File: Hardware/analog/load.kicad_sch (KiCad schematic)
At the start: 41 parts

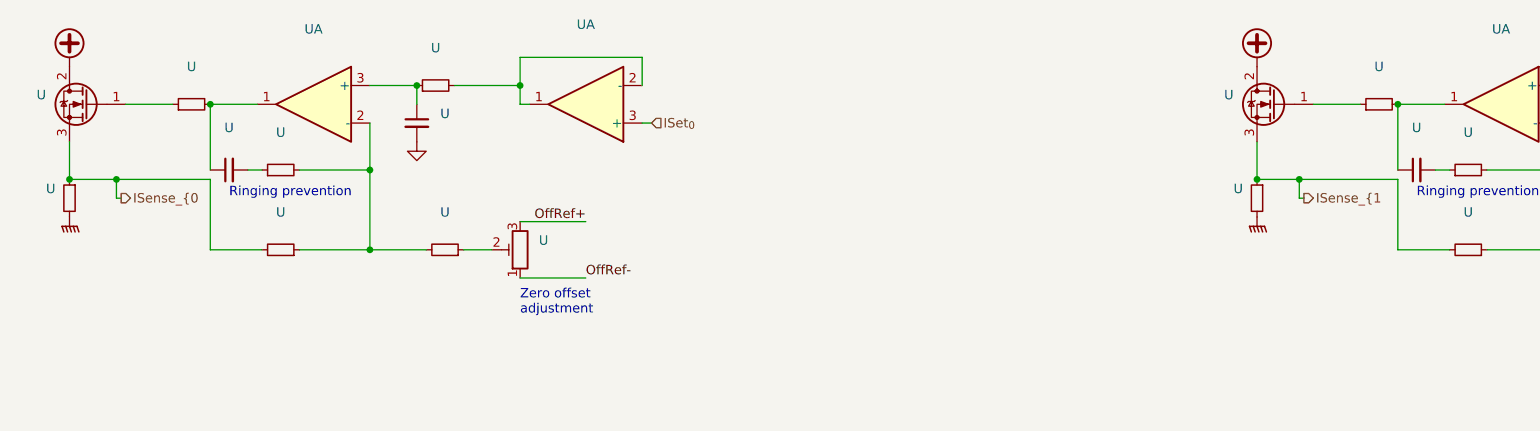
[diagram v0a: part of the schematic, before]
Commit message: Analog board tweaks
- Moved a few traces and components around to accomodate other changes
  in the controller stuff, preparation for some sort of cleanup

- Aesthetic moves of labels on controller board
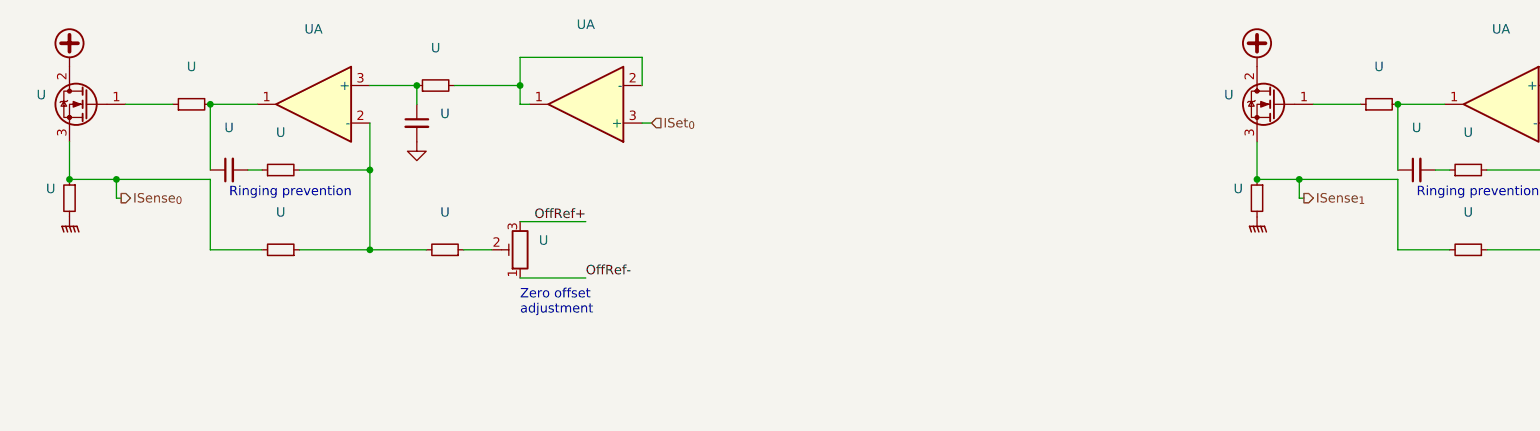
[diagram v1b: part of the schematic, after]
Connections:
- net ISense_{0 renamed ISense_{0}
- net ISense_{1 renamed ISense_{1}
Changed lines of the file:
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@@
     (effects (font (size 1.27 1.27)) (justify left))
   )
-  (hierarchical_label "ISense_{0" (shape output) (at 39.37 43.18 0) (fields_autoplaced)
+  (hierarchical_label "ISense_{0}" (shape output) (at 39.37 43.18 0) (fields_autoplaced)
     (effects (font (size 1.27 1.27)) (justify left))
   )
-  (hierarchical_label "ISense_{1" (shape output) (at 199.39 43.18 0) (fields_autoplaced)
+  (hierarchical_label "ISense_{1}" (shape output) (at 199.39 43.18 0) (fields_autoplaced)
     (effects (font (size 1.27 1.27)) (justify left))
   )

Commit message: Mostly finished up analog load board
- Finished routing most signals

- Connected relay drive to bonus I2C GPIO controller, and routed the
  rest of the voltage sense stuff

- Routed the reset signal to the DAC, so that when the board is reset,
  the current output will be reset to zero as well without processor
  intervention

- Replaced most passives with 0603/1608 size
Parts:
- U: MPN CR0805-JW-102ELF -> (none)
- U: MPN WR08X101-JTL -> (none)
- U: MPN 260-4.7M-RC -> (none)
- U: MPN CL21B223KBANNNC -> (none)
- U: MPN CR0805-FX-4991ELF -> (none)
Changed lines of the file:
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@@
       (effects (font (size 1.27 1.27)) hide)
     )
-    (property "MPN" "CR0805-JW-102ELF" (id 4) (at 60.96 39.37 90)
+    (property "MPN" "" (id 4) (at 60.96 39.37 90)
       (effects (font (size 1.27 1.27)) hide)
     )
@@
       (effects (font (size 1.27 1.27)) hide)
     )
-    (property "MPN" "CR0805-JW-102ELF" (id 4) (at 221.615 50.165 90)
+    (property "MPN" "" (id 4) (at 221.615 50.165 90)
       (effects (font (size 1.27 1.27)) hide)
     )
@@
       (effects (font (size 1.27 1.27)) hide)
     )
-    (property "MPN" "WR08X101-JTL" (id 4) (at 209.55 30.48 90)
+    (property "MPN" "" (id 4) (at 209.55 30.48 90)
       (effects (font (size 1.27 1.27)) hide)
     )
@@
       (effects (font (size 1.27 1.27)) hide)
     )
-    (property "MPN" "CR0805-JW-102ELF" (id 4) (at 221.615 39.37 90)
+    (property "MPN" "" (id 4) (at 221.615 39.37 90)
       (effects (font (size 1.27 1.27)) hide)
     )
@@
       (effects (font (size 1.27 1.27)) hide)
     )
-    (property "MPN" "260-4.7M-RC" (id 4) (at 243.84 50.165 90)
+    (property "MPN" "" (id 4) (at 243.84 50.165 90)
       (effects (font (size 1.27 1.27)) hide)
     )
@@
       (effects (font (size 1.27 1.27)) hide)
     )
-    (property "MPN" "CL21B223KBANNNC" (id 4) (at 79.375 33.02 0)
+    (property "MPN" "" (id 4) (at 79.375 33.02 0)
       (effects (font (size 1.27 1.27)) hide)
     )
@@
       (effects (font (size 1.27 1.27)) hide)
     )
-    (property "MPN" "CR0805-FX-4991ELF" (id 4) (at 81.915 27.94 90)
+    (property "MPN" "" (id 4) (at 81.915 27.94 90)
       (effects (font (size 1.27 1.27)) hide)
     )
@@
       (effects (font (size 1.27 1.27)) hide)
     )
-    (property "MPN" "CR0805-JW-102ELF" (id 4) (at 60.96 50.165 90)
+    (property "MPN" "" (id 4) (at 60.96 50.165 90)
       (effects (font (size 1.27 1.27)) hide)
     )
@@
       (effects (font (size 1.27 1.27)) hide)
     )
-    (property "MPN" "CR0805-FX-4991ELF" (id 4) (at 242.57 27.94 90)
+    (property "MPN" "" (id 4) (at 242.57 27.94 90)
       (effects (font (size 1.27 1.27)) hide)
     )
@@
       (effects (font (size 1.27 1.27)) hide)
     )
-    (property "MPN" "WR08X101-JTL" (id 4) (at 48.895 30.48 90)
+    (property "MPN" "" (id 4) (at 48.895 30.48 90)
       (effects (font (size 1.27 1.27)) hide)
     )
@@
       (effects (font (size 1.27 1.27)) hide)
     )
-    (property "MPN" "CL21B223KBANNNC" (id 4) (at 240.03 33.02 0)
+    (property "MPN" "" (id 4) (at 240.03 33.02 0)
       (effects (font (size 1.27 1.27)) hide)
     )
@@
       (effects (font (size 1.27 1.27)) hide)
     )
-    (property "MPN" "CR0805-JW-102ELF" (id 4) (at 123.825 139.065 0)
+    (property "MPN" "" (id 4) (at 123.825 139.065 0)
       (effects (font (size 1.27 1.27)) hide)
     )
@@
       (effects (font (size 1.27 1.27)) hide)
     )
-    (property "MPN" "CR0805-JW-102ELF" (id 4) (at 101.6 139.065 0)
+    (property "MPN" "" (id 4) (at 101.6 139.065 0)
       (effects (font (size 1.27 1.27)) hide)
     )
@@
       (effects (font (size 1.27 1.27)) hide)
     )
-    (property "MPN" "260-4.7M-RC" (id 4) (at 83.185 50.165 90)
-      (effects (font (size 1.27 1.27)) hide)
-    )
+    (property "MPN" "" (id 4) (at 83.185 50.165 90)
+      (effects (font (size 1.27 1.27)) hide)
+    )

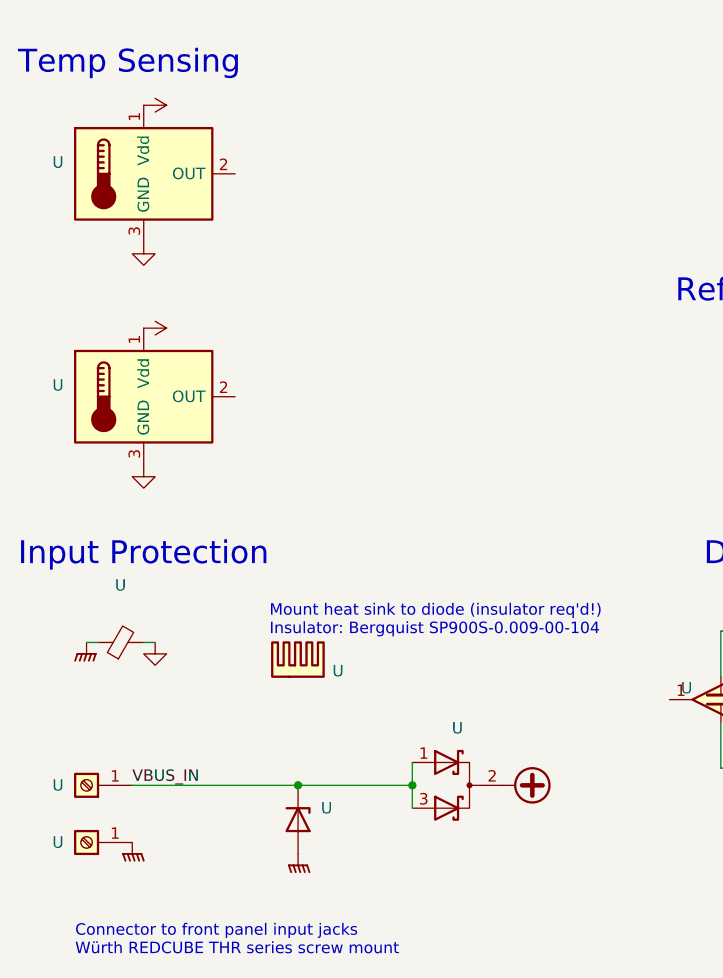
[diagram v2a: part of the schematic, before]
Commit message: Temperature sensing & cleanup for analog board
- Added the auxiliary temperature sensing ADC, and routed it to the
  analog temperature sensors on the front and rear of the MOSFET
  heatsink

- Added an LM75 sensor to measure the analog board ambient temperature
  (for better temperature control/fan control)

  This may end up being a DNP item if it's not really useful or
  otherwise necessary.

- Fixes to a few symbols (namely pin directions) to pass ERC
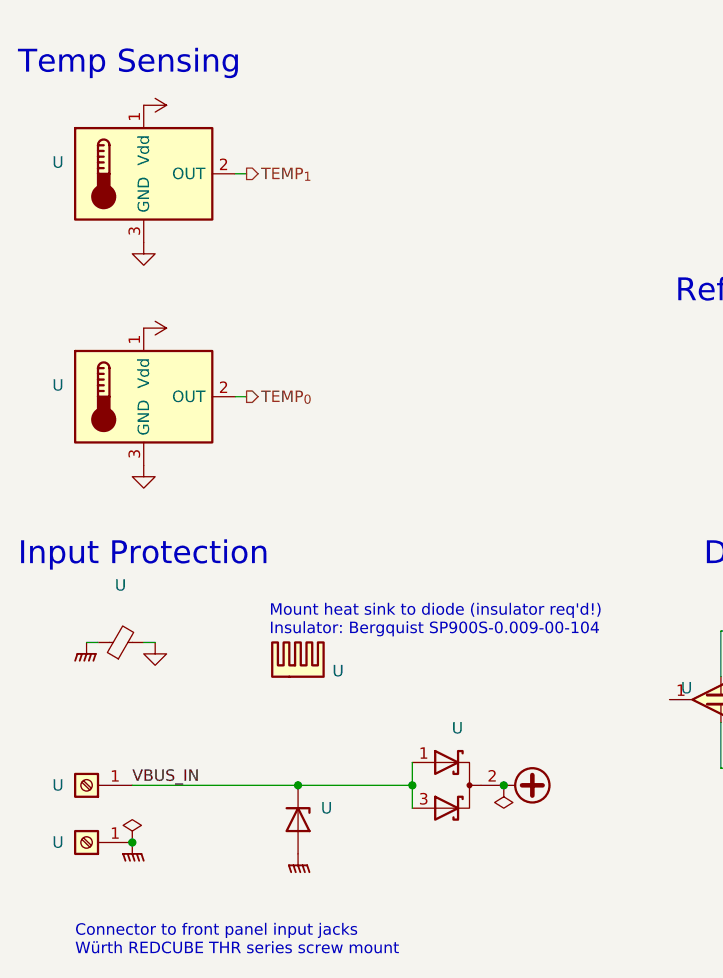
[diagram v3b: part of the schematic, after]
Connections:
- net TEMP_{1}: now reaches U.2 (OUT)
- net TEMP_{0}: now reaches U.2 (OUT)
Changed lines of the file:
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@@
   (junction (at 123.825 136.525) (diameter 0) (color 0 0 0 0)
   )
+  (junction (at 73.025 176.53) (diameter 0) (color 0 0 0 0)
+  )
   (junction (at 240.03 27.94) (diameter 0) (color 0 0 0 0)
   )
   (junction (at 51.435 30.48) (diameter 0) (color 0 0 0 0)
   )
+  (junction (at 31.75 182.88) (diameter 0) (color 0 0 0 0)
+  )
   (junction (at 93.345 27.94) (diameter 0) (color 0 0 0 0)
   )
@@
     (stroke (width 0) (type default))
   )
+  (wire (pts (xy 43.18 133.35) (xy 44.45 133.35))
+    (stroke (width 0) (type default))
+  )
   (wire (pts (xy 79.375 27.94) (xy 79.375 30.48))
     (stroke (width 0) (type default))
@@
   )
   (wire (pts (xy 73.025 39.37) (xy 73.025 50.165))
+    (stroke (width 0) (type default))
+  )
+  (wire (pts (xy 43.18 108.585) (xy 44.45 108.585))
     (stroke (width 0) (type default))
   )
@@
     (effects (font (size 1.27 1.27)) (justify left))
   )
+  (hierarchical_label "TEMP_{1}" (shape output) (at 44.45 108.585 0) (fields_autoplaced)
+    (effects (font (size 1.27 1.27)) (justify left))
+  )
   (hierarchical_label "ISense_{0}" (shape output) (at 39.37 43.18 0) (fields_autoplaced)
+    (effects (font (size 1.27 1.27)) (justify left))
+  )
+  (hierarchical_label "TEMP_{0}" (shape output) (at 44.45 133.35 0) (fields_autoplaced)
     (effects (font (size 1.27 1.27)) (justify left))
   )
@@
     (pin "2")
   )
+  (symbol (lib_id "power:PWR_FLAG") (at 73.025 176.53 180) (unit 1)
+    (in_bom yes) (on_board yes) (fields_autoplaced)
+    (default_instance (reference "#FLG") (unit 1) (value "PWR_FLAG") (footprint ""))
+    (property "Reference" "#FLG" (id 0) (at 73.025 178.435 0)
+      (effects (font (size 1.27 1.27)) hide)
+    )
+    (property "Value" "PWR_FLAG" (id 1) (at 73.025 181.61 0)
+      (effects (font (size 1.27 1.27)) hide)
+    )
+    (property "Footprint" "" (id 2) (at 73.025 176.53 0)
+      (effects (font (size 1.27 1.27)) hide)
+    )
+    (property "Datasheet" "~" (id 3) (at 73.025 176.53 0)
+      (effects (font (size 1.27 1.27)) hide)
+    )
+    (pin "1")
+  )
   (symbol (lib_id "power:GND") (at 101.6 130.175 0) (mirror x) (unit 1)
     (in_bom yes) (on_board yes)
@@
     (pin "2")
   )
+  (symbol (lib_id "power:PWR_FLAG") (at 31.75 182.88 0) (unit 1)
+    (in_bom yes) (on_board yes) (fields_autoplaced)
+    (default_instance (reference "#FLG") (unit 1) (value "PWR_FLAG") (footprint ""))
+    (property "Reference" "#FLG" (id 0) (at 31.75 180.975 0)
+      (effects (font (size 1.27 1.27)) hide)
+    )
+    (property "Value" "PWR_FLAG" (id 1) (at 31.75 177.8 0)
+      (effects (font (size 1.27 1.27)) hide)
+    )
+    (property "Footprint" "" (id 2) (at 31.75 182.88 0)
+      (effects (font (size 1.27 1.27)) hide)
+    )
+    (property "Datasheet" "~" (id 3) (at 31.75 182.88 0)
+      (effects (font (size 1.27 1.27)) hide)
+    )
+    (pin "1")
+  )
   (symbol (lib_id "Reference_Voltage:TL431DBZ") (at 123.825 133.985 270) (mirror x) (unit 1)
